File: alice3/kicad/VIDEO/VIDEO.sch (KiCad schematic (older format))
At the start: 8 parts, among them SW1 SW_PUSH, U1 Propeller_P8X32A-D40, U2 VGA_daughter_board, U3 24LC256, U4 Propeller_Plug, Y1 5 MHz

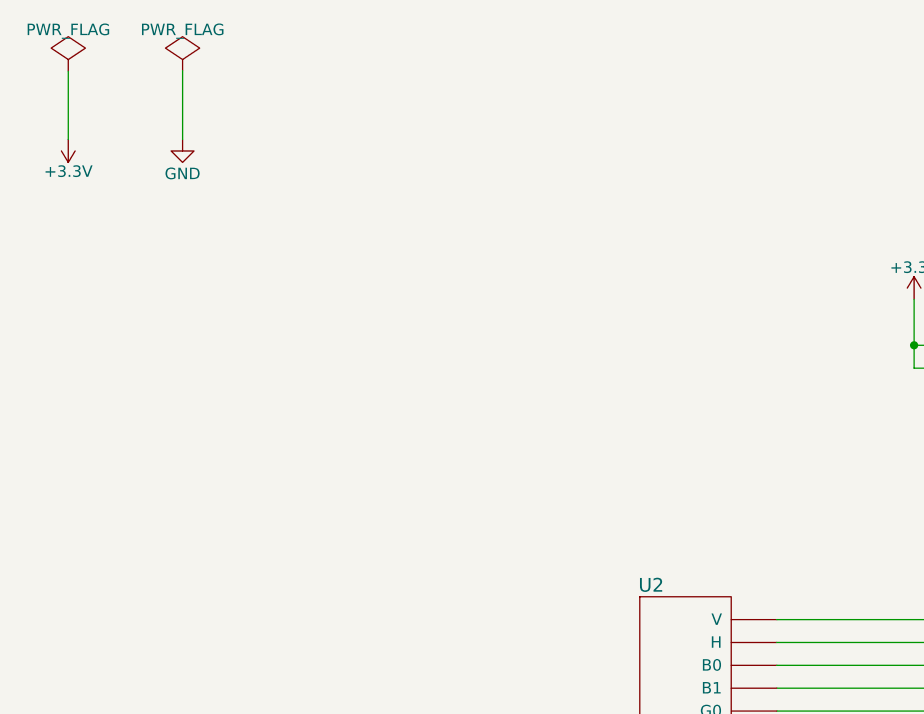
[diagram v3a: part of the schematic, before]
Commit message: Add 3.3 V regulator and power LED.
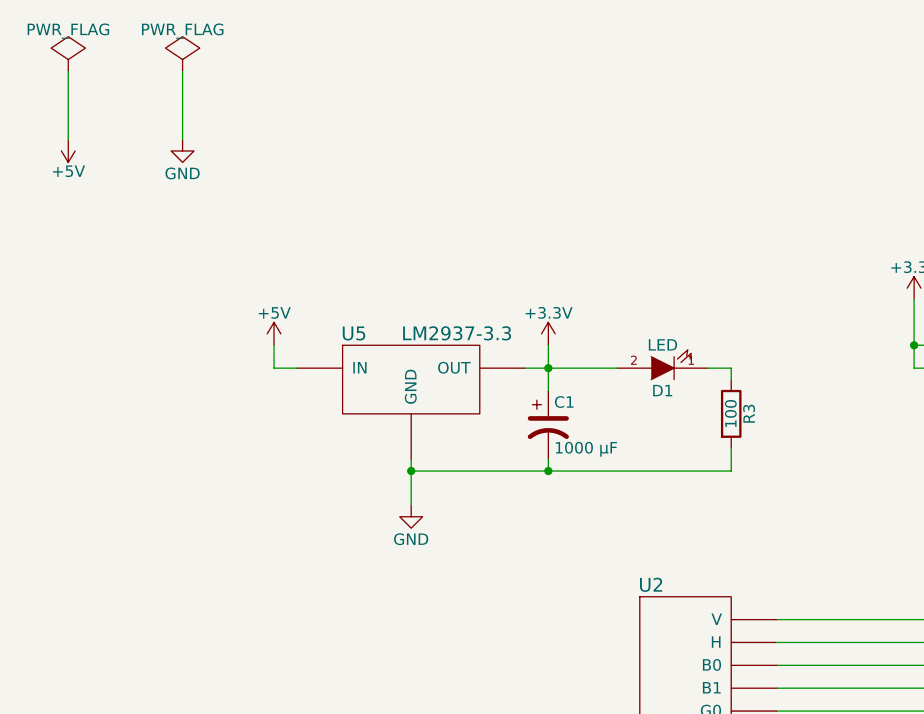
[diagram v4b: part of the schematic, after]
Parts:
- added C1: 1000 µF, symbol CP1
- added D1: LED, symbol LED
- added R3: 100, symbol R
- added U5: LM2937-3.3, symbol LM2937-3.3
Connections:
- net +3V3: now also C1.1, D1.2 (A), U5.~ (OUT)
- net GND: now also C1.2, R3.2, U5.~ (OUT)
- new net: D1.1 (K), R3.1
- new net +5V: U5.~ (OUT)
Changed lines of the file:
@@
 LIBS:24lc256
 LIBS:propeller_plug
+LIBS:lm2937-3-3
 LIBS:VIDEO-cache
 EELAYER 25 0
@@
 $EndComp
 $Comp
-L GND #PWR4
+L GND #PWR7
 U 1 1 566E4A0D
 P 4700 4800
-F 0 "#PWR4" H 4700 4550 50  0001 C CNN
+F 0 "#PWR7" H 4700 4550 50  0001 C CNN
 F 1 "GND" H 4700 4650 50  0000 C CNN
 F 2 "" H 4700 4800 50  0000 C CNN
@@
 $EndComp
 $Comp
-L +3.3V #PWR3
+L +3.3V #PWR6
 U 1 1 566E4A37
 P 4700 2200
-F 0 "#PWR3" H 4700 2050 50  0001 C CNN
+F 0 "#PWR6" H 4700 2050 50  0001 C CNN
 F 1 "+3.3V" H 4700 2340 50  0000 C CNN
 F 2 "" H 4700 2200 50  0000 C CNN
@@
 $EndComp
 $Comp
-L GND #PWR5
+L GND #PWR8
 U 1 1 566E4B37
 P 6300 2500
-F 0 "#PWR5" H 6300 2250 50  0001 C CNN
+F 0 "#PWR8" H 6300 2250 50  0001 C CNN
 F 1 "GND" H 6300 2350 50  0000 C CNN
 F 2 "" H 6300 2500 50  0000 C CNN
@@
 $EndComp
 $Comp
-L +3.3V #PWR6
+L +3.3V #PWR9
 U 1 1 566E4B67
 P 6500 1800
-F 0 "#PWR6" H 6500 1650 50  0001 C CNN
+F 0 "#PWR9" H 6500 1650 50  0001 C CNN
 F 1 "+3.3V" H 6500 1940 50  0000 C CNN
 F 2 "" H 6500 1800 50  0000 C CNN
@@
 $EndComp
 $Comp
-L GND #PWR9
+L GND #PWR12
 U 1 1 566E4C07
 P 7250 2500
-F 0 "#PWR9" H 7250 2250 50  0001 C CNN
+F 0 "#PWR12" H 7250 2250 50  0001 C CNN
 F 1 "GND" H 7250 2350 50  0000 C CNN
 F 2 "" H 7250 2500 50  0000 C CNN
@@
 $EndComp
 $Comp
-L +3.3V #PWR1
-U 1 1 566E4D29
-P 1000 1500
-F 0 "#PWR1" H 1000 1350 50  0001 C CNN
-F 1 "+3.3V" H 1000 1640 50  0000 C CNN
-F 2 "" H 1000 1500 50  0000 C CNN
-F 3 "" H 1000 1500 50  0000 C CNN
-	1    1000 1500
-	-1   0    0    1
-$EndComp
-$Comp
 L GND #PWR2
 U 1 1 566E4D40
@@
 $EndComp
 $Comp
-L GND #PWR8
+L GND #PWR11
 U 1 1 5681F164
 P 6950 4500
-F 0 "#PWR8" H 6950 4250 50  0001 C CNN
+F 0 "#PWR11" H 6950 4250 50  0001 C CNN
 F 1 "GND" H 6950 4350 50  0000 C CNN
 F 2 "" H 6950 4500 50  0000 C CNN
@@
 $EndComp
 $Comp
-L +3.3V #PWR10
+L +3.3V #PWR13
 U 1 1 5681F2C2
 P 8050 3950
-F 0 "#PWR10" H 8050 3800 50  0001 C CNN
+F 0 "#PWR13" H 8050 3800 50  0001 C CNN
 F 1 "+3.3V" H 8050 4090 50  0000 C CNN
 F 2 "" H 8050 3950 50  0000 C CNN
@@
 $EndComp
 $Comp
-L GND #PWR11
+L GND #PWR14
 U 1 1 5681F2E8
 P 8300 4250
-F 0 "#PWR11" H 8300 4000 50  0001 C CNN
+F 0 "#PWR14" H 8300 4000 50  0001 C CNN
 F 1 "GND" H 8300 4100 50  0000 C CNN
 F 2 "" H 8300 4250 50  0000 C CNN
@@
 $EndComp
 $Comp
-L +3.3V #PWR7
+L +3.3V #PWR10
 U 1 1 5681F435
 P 6700 3700
-F 0 "#PWR7" H 6700 3550 50  0001 C CNN
+F 0 "#PWR10" H 6700 3550 50  0001 C CNN
 F 1 "+3.3V" H 6700 3840 50  0000 C CNN
 F 2 "" H 6700 3700 50  0000 C CNN
@@
 	7250 2400 7250 2500
 Connection ~ 7250 2400
+$Comp
+L LM2937-3.3 U5
+U 1 1 5681F8BE
+P 2500 2550
+F 0 "U5" H 2250 2750 60  0000 C CNN
+F 1 "LM2937-3.3" H 2700 2750 60  0000 C CNN
+F 2 "" H 2500 2550 60  0000 C CNN
+F 3 "" H 2500 2550 60  0000 C CNN
+	1    2500 2550
+	1    0    0    -1
+$EndComp
+$Comp
+L GND #PWR4
+U 1 1 5681F91B
+P 2500 3100
+F 0 "#PWR4" H 2500 2850 50  0001 C CNN
+F 1 "GND" H 2500 2950 50  0000 C CNN
+F 2 "" H 2500 3100 50  0000 C CNN
+F 3 "" H 2500 3100 50  0000 C CNN
+	1    2500 3100
+	1    0    0    -1
+$EndComp
+Wire Wire Line
+	2500 3100 2500 2900
+$Comp
+L +5V #PWR3
+U 1 1 5681FA03
+P 1900 2400
+F 0 "#PWR3" H 1900 2250 50  0001 C CNN
+F 1 "+5V" H 1900 2540 50  0000 C CNN
+F 2 "" H 1900 2400 50  0000 C CNN
+F 3 "" H 1900 2400 50  0000 C CNN
+	1    1900 2400
+	1    0    0    -1
+$EndComp
+$Comp
+L +3.3V #PWR5
+U 1 1 5681FA32
+P 3100 2400
+F 0 "#PWR5" H 3100 2250 50  0001 C CNN
+F 1 "+3.3V" H 3100 2540 50  0000 C CNN
+F 2 "" H 3100 2400 50  0000 C CNN
+F 3 "" H 3100 2400 50  0000 C CNN
+	1    3100 2400
+	1    0    0    -1
+$EndComp
+$Comp
+L +5V #PWR1
+U 1 1 5681FAF3
+P 1000 1500
+F 0 "#PWR1" H 1000 1350 50  0001 C CNN
+F 1 "+5V" H 1000 1640 50  0000 C CNN
+F 2 "" H 1000 1500 50  0000 C CNN
+F 3 "" H 1000 1500 50  0000 C CNN
+	1    1000 1500
+	-1   0    0    1
+$EndComp
+Wire Wire Line
+	2000 2500 1900 2500
+Wire Wire Line
+	1900 2500 1900 2400
+$Comp
+L CP1 C1
+U 1 1 5681FB9D
+P 3100 2750
+F 0 "C1" H 3125 2850 50  0000 L CNN
+F 1 "1000 µF" H 3125 2650 50  0000 L CNN
+F 2 "" H 3100 2750 50  0000 C CNN
+F 3 "" H 3100 2750 50  0000 C CNN
+	1    3100 2750
+	1    0    0    -1
+$EndComp
+Wire Wire Line
+	3000 2500 3400 2500
+Wire Wire Line
+	3100 2400 3100 2600
+Connection ~ 3100 2500
+Wire Wire Line
+	3100 2900 3100 2950
+Wire Wire Line
+	2500 2950 3900 2950
+Connection ~ 2500 2950
+$Comp
+L LED D1
+U 1 1 5681FD4E
+P 3600 2500
+F 0 "D1" H 3600 2600 50  0000 C CNN
+F 1 "LED" H 3600 2400 50  0000 C CNN
+F 2 "" H 3600 2500 50  0000 C CNN
+F 3 "" H 3600 2500 50  0000 C CNN
+	1    3600 2500
+	-1   0    0    1
+$EndComp
+$Comp
+L R R3
+U 1 1 5681FD9C
+P 3900 2700
+F 0 "R3" V 3980 2700 50  0000 C CNN
+F 1 "100" V 3900 2700 50  0000 C CNN
+F 2 "" V 3830 2700 50  0000 C CNN
+F 3 "" H 3900 2700 50  0000 C CNN
+	1    3900 2700
+	1    0    0    -1
+$EndComp
+Wire Wire Line
+	3800 2500 3900 2500
+Wire Wire Line
+	3900 2500 3900 2550
+Wire Wire Line
+	3900 2950 3900 2850
+Connection ~ 3100 2950
 $EndSCHEMATC

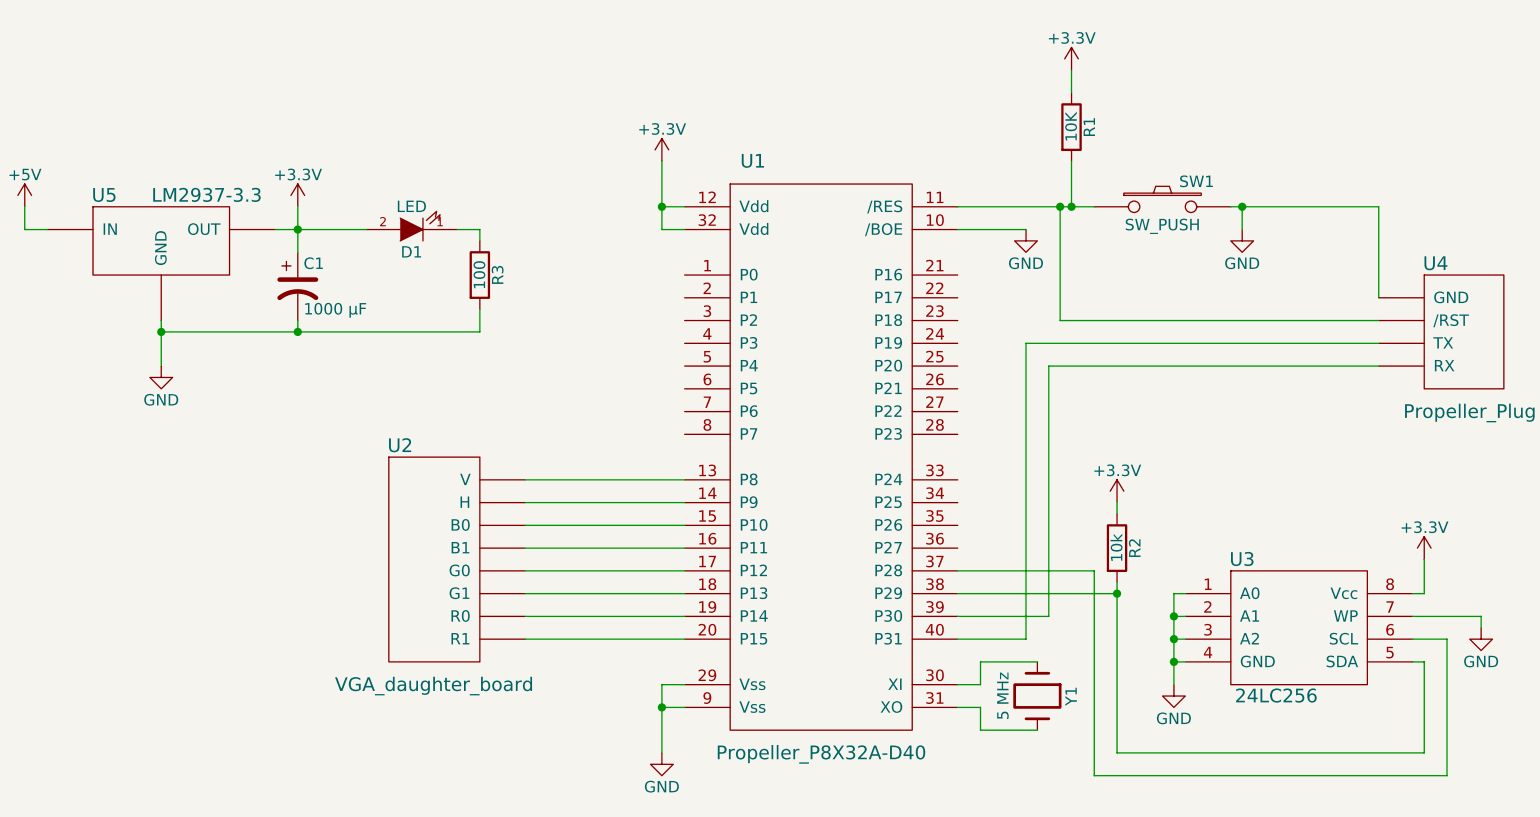
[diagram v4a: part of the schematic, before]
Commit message: Add debug LED to video board.
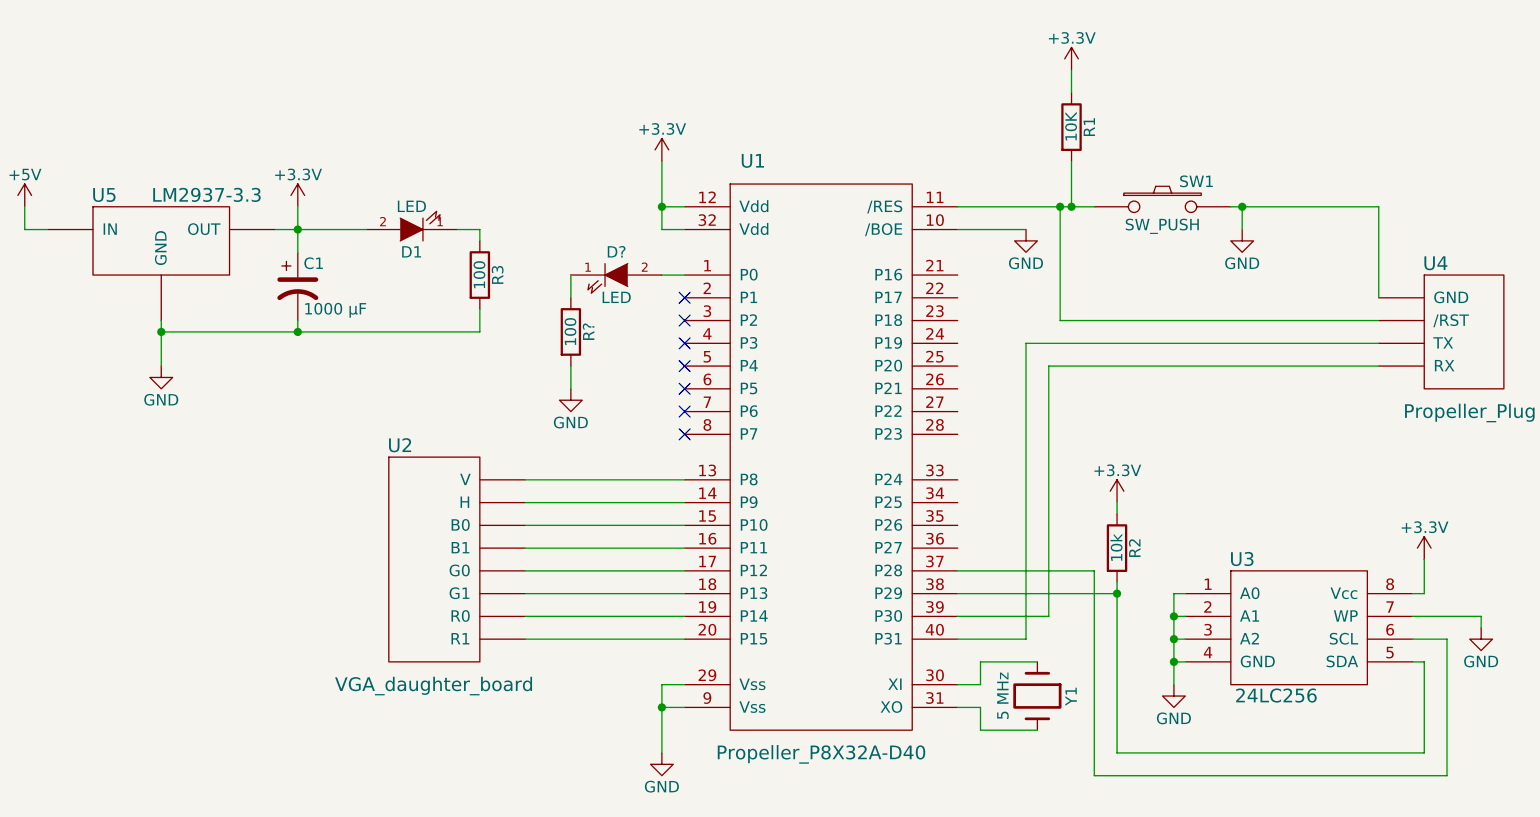
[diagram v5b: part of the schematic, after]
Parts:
- added D?: LED, symbol LED
- added R?: 100, symbol R
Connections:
- net GND: now also R?.2
- net at U1.1 (P0): now also D?.2 (A)
- new net: D?.1 (K), R?.1
- no-connect marks 0 -> 7
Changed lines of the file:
@@
 $EndComp
 $Comp
-L GND #PWR7
+L GND #PWR01
 U 1 1 566E4A0D
 P 4700 4800
-F 0 "#PWR7" H 4700 4550 50  0001 C CNN
+F 0 "#PWR01" H 4700 4550 50  0001 C CNN
 F 1 "GND" H 4700 4650 50  0000 C CNN
 F 2 "" H 4700 4800 50  0000 C CNN
@@
 $EndComp
 $Comp
-L +3.3V #PWR6
+L +3.3V #PWR02
 U 1 1 566E4A37
 P 4700 2200
-F 0 "#PWR6" H 4700 2050 50  0001 C CNN
+F 0 "#PWR02" H 4700 2050 50  0001 C CNN
 F 1 "+3.3V" H 4700 2340 50  0000 C CNN
 F 2 "" H 4700 2200 50  0000 C CNN
@@
 $EndComp
 $Comp
-L GND #PWR8
+L GND #PWR03
 U 1 1 566E4B37
 P 6300 2500
-F 0 "#PWR8" H 6300 2250 50  0001 C CNN
+F 0 "#PWR03" H 6300 2250 50  0001 C CNN
 F 1 "GND" H 6300 2350 50  0000 C CNN
 F 2 "" H 6300 2500 50  0000 C CNN
@@
 $EndComp
 $Comp
-L +3.3V #PWR9
+L +3.3V #PWR04
 U 1 1 566E4B67
 P 6500 1800
-F 0 "#PWR9" H 6500 1650 50  0001 C CNN
+F 0 "#PWR04" H 6500 1650 50  0001 C CNN
 F 1 "+3.3V" H 6500 1940 50  0000 C CNN
 F 2 "" H 6500 1800 50  0000 C CNN
@@
 $EndComp
 $Comp
-L GND #PWR12
+L GND #PWR05
 U 1 1 566E4C07
 P 7250 2500
-F 0 "#PWR12" H 7250 2250 50  0001 C CNN
+F 0 "#PWR05" H 7250 2250 50  0001 C CNN
 F 1 "GND" H 7250 2350 50  0000 C CNN
 F 2 "" H 7250 2500 50  0000 C CNN
@@
 $EndComp
 $Comp
-L PWR_FLAG #FLG1
+L PWR_FLAG #FLG06
 U 1 1 566E4C94
 P 1000 1200
-F 0 "#FLG1" H 1000 1295 50  0001 C CNN
+F 0 "#FLG06" H 1000 1295 50  0001 C CNN
 F 1 "PWR_FLAG" H 1000 1380 50  0000 C CNN
 F 2 "" H 1000 1200 50  0000 C CNN
@@
 $EndComp
 $Comp
-L PWR_FLAG #FLG2
+L PWR_FLAG #FLG07
 U 1 1 566E4CCE
 P 1500 1200
-F 0 "#FLG2" H 1500 1295 50  0001 C CNN
+F 0 "#FLG07" H 1500 1295 50  0001 C CNN
 F 1 "PWR_FLAG" H 1500 1380 50  0000 C CNN
 F 2 "" H 1500 1200 50  0000 C CNN
@@
 $EndComp
 $Comp
-L GND #PWR2
+L GND #PWR08
 U 1 1 566E4D40
 P 1500 1500
-F 0 "#PWR2" H 1500 1250 50  0001 C CNN
+F 0 "#PWR08" H 1500 1250 50  0001 C CNN
 F 1 "GND" H 1500 1350 50  0000 C CNN
 F 2 "" H 1500 1500 50  0000 C CNN
@@
 $EndComp
 $Comp
-L GND #PWR11
+L GND #PWR09
 U 1 1 5681F164
 P 6950 4500
-F 0 "#PWR11" H 6950 4250 50  0001 C CNN
+F 0 "#PWR09" H 6950 4250 50  0001 C CNN
 F 1 "GND" H 6950 4350 50  0000 C CNN
 F 2 "" H 6950 4500 50  0000 C CNN
@@
 $EndComp
 $Comp
-L +3.3V #PWR13
+L +3.3V #PWR010
 U 1 1 5681F2C2
 P 8050 3950
-F 0 "#PWR13" H 8050 3800 50  0001 C CNN
+F 0 "#PWR010" H 8050 3800 50  0001 C CNN
 F 1 "+3.3V" H 8050 4090 50  0000 C CNN
 F 2 "" H 8050 3950 50  0000 C CNN
@@
 $EndComp
 $Comp
-L GND #PWR14
+L GND #PWR011
 U 1 1 5681F2E8
 P 8300 4250
-F 0 "#PWR14" H 8300 4000 50  0001 C CNN
+F 0 "#PWR011" H 8300 4000 50  0001 C CNN
 F 1 "GND" H 8300 4100 50  0000 C CNN
 F 2 "" H 8300 4250 50  0000 C CNN
@@
 $EndComp
 $Comp
-L +3.3V #PWR10
+L +3.3V #PWR012
 U 1 1 5681F435
 P 6700 3700
-F 0 "#PWR10" H 6700 3550 50  0001 C CNN
+F 0 "#PWR012" H 6700 3550 50  0001 C CNN
 F 1 "+3.3V" H 6700 3840 50  0000 C CNN
 F 2 "" H 6700 3700 50  0000 C CNN
@@
 	4800 4500 4700 4500
 Wire Wire Line
-	4700 4500 4700 4800
+	4700 4500 4700 4600
+Wire Wire Line
+	4700 4600 4700 4800
 Wire Wire Line
 	4800 4600 4700 4600
@@
 	4700 2500 4800 2500
 Wire Wire Line
-	4700 2200 4700 2500
+	4700 2200 4700 2400
+Wire Wire Line
+	4700 2400 4700 2500
 Wire Wire Line
 	4800 2400 4700 2400
@@
 	6500 1900 6500 1800
 Wire Wire Line
-	6000 2400 6600 2400
+	6000 2400 6450 2400
+Wire Wire Line
+	6450 2400 6500 2400
+Wire Wire Line
+	6500 2400 6600 2400
 Wire Wire Line
 	6500 2400 6500 2200
@@
 	7000 4100 6950 4100
 Wire Wire Line
-	6950 4100 6950 4500
+	6950 4100 6950 4200
+Wire Wire Line
+	6950 4200 6950 4300
+Wire Wire Line
+	6950 4300 6950 4400
+Wire Wire Line
+	6950 4400 6950 4500
 Wire Wire Line
 	7000 4200 6950 4200
@@
 	8050 4800 6700 4800
 Wire Wire Line
-	6700 4800 6700 4050
+	6700 4800 6700 4100
+Wire Wire Line
+	6700 4100 6700 4050
 Wire Wire Line
 	6700 4100 6000 4100
@@
 	7850 2400 7850 2800
 Wire Wire Line
-	7200 2400 7850 2400
+	7200 2400 7250 2400
+Wire Wire Line
+	7250 2400 7850 2400
 Wire Wire Line
 	7250 2400 7250 2500
@@
 $EndComp
 $Comp
-L GND #PWR4
+L GND #PWR013
 U 1 1 5681F91B
 P 2500 3100
-F 0 "#PWR4" H 2500 2850 50  0001 C CNN
+F 0 "#PWR013" H 2500 2850 50  0001 C CNN
 F 1 "GND" H 2500 2950 50  0000 C CNN
 F 2 "" H 2500 3100 50  0000 C CNN
@@
 $EndComp
 Wire Wire Line
-	2500 3100 2500 2900
-$Comp
-L +5V #PWR3
+	2500 3100 2500 2950
+Wire Wire Line
+	2500 2950 2500 2900
+$Comp
+L +5V #PWR014
 U 1 1 5681FA03
 P 1900 2400
-F 0 "#PWR3" H 1900 2250 50  0001 C CNN
+F 0 "#PWR014" H 1900 2250 50  0001 C CNN
 F 1 "+5V" H 1900 2540 50  0000 C CNN
 F 2 "" H 1900 2400 50  0000 C CNN
@@
 $EndComp
 $Comp
-L +3.3V #PWR5
+L +3.3V #PWR015
 U 1 1 5681FA32
 P 3100 2400
-F 0 "#PWR5" H 3100 2250 50  0001 C CNN
+F 0 "#PWR015" H 3100 2250 50  0001 C CNN
 F 1 "+3.3V" H 3100 2540 50  0000 C CNN
 F 2 "" H 3100 2400 50  0000 C CNN
@@
 $EndComp
 $Comp
-L +5V #PWR1
+L +5V #PWR016
 U 1 1 5681FAF3
 P 1000 1500
-F 0 "#PWR1" H 1000 1350 50  0001 C CNN
+F 0 "#PWR016" H 1000 1350 50  0001 C CNN
 F 1 "+5V" H 1000 1640 50  0000 C CNN
 F 2 "" H 1000 1500 50  0000 C CNN
@@
 $EndComp
 Wire Wire Line
-	3000 2500 3400 2500
-Wire Wire Line
-	3100 2400 3100 2600
+	3000 2500 3100 2500
+Wire Wire Line
+	3100 2500 3400 2500
+Wire Wire Line
+	3100 2400 3100 2500
+Wire Wire Line
+	3100 2500 3100 2600
 Connection ~ 3100 2500
 Wire Wire Line
 	3100 2900 3100 2950
 Wire Wire Line
-	2500 2950 3900 2950
+	2500 2950 3100 2950
+Wire Wire Line
+	3100 2950 3900 2950
 Connection ~ 2500 2950
 $Comp
@@
 	3900 2950 3900 2850
 Connection ~ 3100 2950
+$Comp
+L LED D?
+U 1 1 56821EAA
+P 4500 2700
+F 0 "D?" H 4500 2800 50  0000 C CNN
+F 1 "LED" H 4500 2600 50  0000 C CNN
+F 2 "" H 4500 2700 50  0000 C CNN
+F 3 "" H 4500 2700 50  0000 C CNN
+	1    4500 2700
+	1    0    0    -1
+$EndComp
+$Comp
+L R R?
+U 1 1 56821F00
+P 4300 2950
+F 0 "R?" V 4380 2950 50  0000 C CNN
+F 1 "100" V 4300 2950 50  0000 C CNN
+F 2 "" V 4230 2950 50  0000 C CNN
+F 3 "" H 4300 2950 50  0000 C CNN
+	1    4300 2950
+	1    0    0    -1
+$EndComp
+$Comp
+L GND #PWR?
+U 1 1 56821F3F
+P 4300 3200
+F 0 "#PWR?" H 4300 2950 50  0001 C CNN
+F 1 "GND" H 4300 3050 50  0000 C CNN
+F 2 "" H 4300 3200 50  0000 C CNN
+F 3 "" H 4300 3200 50  0000 C CNN
+	1    4300 3200
+	1    0    0    -1
+$EndComp
+Wire Wire Line
+	4300 2800 4300 2700
+Wire Wire Line
+	4700 2700 4800 2700
+Wire Wire Line
+	4300 3200 4300 3100
+NoConn ~ 4800 2800
+NoConn ~ 4800 2900
+NoConn ~ 4800 3000
+NoConn ~ 4800 3100
+NoConn ~ 4800 3200
+NoConn ~ 4800 3300
+NoConn ~ 4800 3400
 $EndSCHEMATC

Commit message: Give names to new components.
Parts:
- gave numbers to parts that had none: 2
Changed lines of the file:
@@
 	4800 4500 4700 4500
 Wire Wire Line
-	4700 4500 4700 4600
-Wire Wire Line
-	4700 4600 4700 4800
+	4700 4500 4700 4800
 Wire Wire Line
 	4800 4600 4700 4600
@@
 	4700 2500 4800 2500
 Wire Wire Line
-	4700 2200 4700 2400
-Wire Wire Line
-	4700 2400 4700 2500
+	4700 2200 4700 2500
 Wire Wire Line
 	4800 2400 4700 2400
@@
 	6500 1900 6500 1800
 Wire Wire Line
-	6000 2400 6450 2400
-Wire Wire Line
-	6450 2400 6500 2400
-Wire Wire Line
-	6500 2400 6600 2400
+	6000 2400 6600 2400
 Wire Wire Line
 	6500 2400 6500 2200
@@
 	7000 4100 6950 4100
 Wire Wire Line
-	6950 4100 6950 4200
-Wire Wire Line
-	6950 4200 6950 4300
-Wire Wire Line
-	6950 4300 6950 4400
-Wire Wire Line
-	6950 4400 6950 4500
+	6950 4100 6950 4500
 Wire Wire Line
 	7000 4200 6950 4200
@@
 	8050 4400 8050 4800
 Wire Wire Line
-	8050 4800 6700 4800
-Wire Wire Line
-	6700 4800 6700 4100
-Wire Wire Line
-	6700 4100 6700 4050
+	6700 4800 8050 4800
+Wire Wire Line
+	6700 4050 6700 4800
 Wire Wire Line
 	6700 4100 6000 4100
@@
 	7850 2400 7850 2800
 Wire Wire Line
-	7200 2400 7250 2400
-Wire Wire Line
-	7250 2400 7850 2400
+	7200 2400 7850 2400
 Wire Wire Line
 	7250 2400 7250 2500
@@
 $EndComp
 Wire Wire Line
-	2500 3100 2500 2950
-Wire Wire Line
-	2500 2950 2500 2900
+	2500 2900 2500 3100
 $Comp
 L +5V #PWR014
@@
 $EndComp
 Wire Wire Line
-	3000 2500 3100 2500
-Wire Wire Line
-	3100 2500 3400 2500
-Wire Wire Line
-	3100 2400 3100 2500
-Wire Wire Line
-	3100 2500 3100 2600
+	3000 2500 3400 2500
+Wire Wire Line
+	3100 2400 3100 2600
 Connection ~ 3100 2500
 Wire Wire Line
 	3100 2900 3100 2950
 Wire Wire Line
-	2500 2950 3100 2950
-Wire Wire Line
-	3100 2950 3900 2950
+	2500 2950 3900 2950
 Connection ~ 2500 2950
 $Comp
@@
 Connection ~ 3100 2950
 $Comp
-L LED D?
+L LED D2
 U 1 1 56821EAA
 P 4500 2700
-F 0 "D?" H 4500 2800 50  0000 C CNN
+F 0 "D2" H 4500 2800 50  0000 C CNN
 F 1 "LED" H 4500 2600 50  0000 C CNN
 F 2 "" H 4500 2700 50  0000 C CNN
@@
 $EndComp
 $Comp
-L R R?
+L R R4
 U 1 1 56821F00
 P 4300 2950
-F 0 "R?" V 4380 2950 50  0000 C CNN
+F 0 "R4" V 4380 2950 50  0000 C CNN
 F 1 "100" V 4300 2950 50  0000 C CNN
 F 2 "" V 4230 2950 50  0000 C CNN
@@
 $EndComp
 $Comp
-L GND #PWR?
+L GND #PWR017
 U 1 1 56821F3F
 P 4300 3200
-F 0 "#PWR?" H 4300 2950 50  0001 C CNN
+F 0 "#PWR017" H 4300 2950 50  0001 C CNN
 F 1 "GND" H 4300 3050 50  0000 C CNN
 F 2 "" H 4300 3200 50  0000 C CNN
